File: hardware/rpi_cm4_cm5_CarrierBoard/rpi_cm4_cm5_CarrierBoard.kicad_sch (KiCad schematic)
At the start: 16 parts, among them J21 61300311121, J22 61300311121, J24 SM04B-SRSS-TB, U37 SN74LVC1G14DBVR

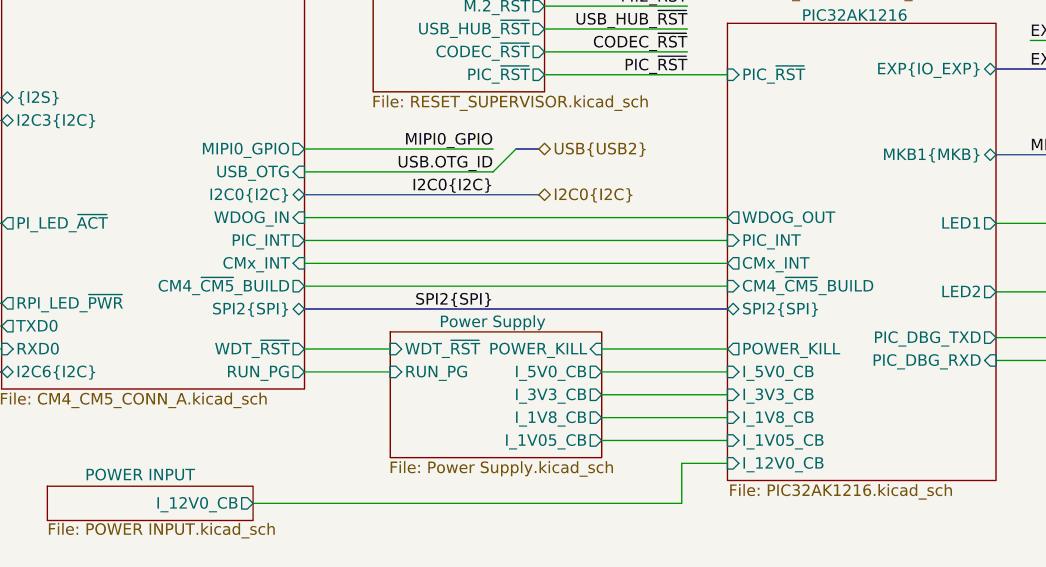
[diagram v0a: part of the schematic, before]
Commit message: Finished implementation of watchdog circuit All possible reset scenarios documented
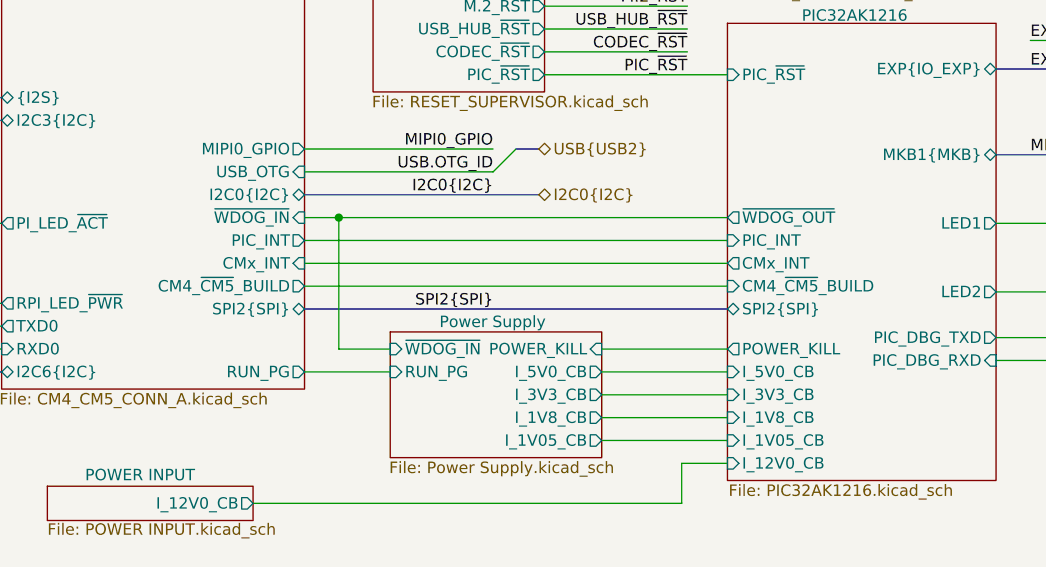
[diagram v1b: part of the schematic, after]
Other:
- sheet CM4_CM5_CONN_A ports: added ~{WDOG_IN}; removed WDOG_IN, WDT_~{RST}
- sheet PIC32AK1216 ports: added ~{WDOG_OUT}; removed WDOG_OUT
- sheet Power Supply ports: added ~{WDOG_IN}; removed WDT_~{RST}
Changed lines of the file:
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@@
 	)
 	(junction
+		(at 159.385 128.905)
+		(diameter 0)
+		(color 0 0 0 0)
+	)
+	(junction
 		(at 195.58 69.85)
 		(diameter 0)
@@
 	(wire
 		(pts
-			(xy 155.575 128.905) (xy 202.565 128.905)
+			(xy 155.575 128.905) (xy 159.385 128.905)
 		)
 		(stroke
@@
 	(wire
 		(pts
+			(xy 159.385 143.51) (xy 165.1 143.51)
+		)
+		(stroke
+			(width 0)
+			(type default)
+		)
+	)
+	(wire
+		(pts
 			(xy 182.245 105.41) (xy 198.12 105.41)
 		)
@@
 		)
 	)
+	(wire
+		(pts
+			(xy 159.385 128.905) (xy 159.385 143.51)
+		)
+		(stroke
+			(width 0)
+			(type default)
+		)
+	)
 	(bus
 		(pts
@@
 	(wire
 		(pts
+			(xy 159.385 128.905) (xy 202.565 128.905)
+		)
+		(stroke
+			(width 0)
+			(type default)
+		)
+	)
+	(wire
+		(pts
 			(xy 104.775 168.275) (xy 104.775 168.91)
 		)
@@
 	(wire
 		(pts
-			(xy 155.575 143.51) (xy 165.1 143.51)
-		)
-		(stroke
-			(width 0)
-			(type default)
-		)
-	)
-	(wire
-		(pts
 			(xy 45.72 91.44) (xy 121.92 91.44)
 		)
@@
 			)
 		)
-		(pin "WDOG_OUT" output
-			(at 202.565 128.905 180)
-			(effects
-				(font
-					(size 1.27 1.27)
-				)
-				(justify left)
-			)
-		)
 		(pin "CMx_INT" output
 			(at 202.565 133.985 180)
@@
 			)
 		)
+		(pin "~{WDOG_OUT}" output
+			(at 202.565 128.905 180)
+			(effects
+				(font
+					(size 1.27 1.27)
+				)
+				(justify left)
+			)
+		)
 		(instances
 			(project "rpi_cm4_cm5_CarrierBoard"
@@
 			)
 		)
-		(pin "WDT_~{RST}" input
+		(pin "~{WDOG_IN}" input
 			(at 165.1 143.51 180)
 			(effects
@@
 			)
 		)
-		(pin "WDOG_IN" input
-			(at 155.575 128.905 0)
-			(effects
-				(font
-					(size 1.27 1.27)
-				)
-				(justify right)
-			)
-		)
 		(pin "I2C3{I2C}" bidirectional
 			(at 121.92 118.11 180)
@@
 			)
 		)
-		(pin "WDT_~{RST}" output
-			(at 155.575 143.51 0)
+		(pin "~{WDOG_IN}" input
+			(at 155.575 128.905 0)
 			(effects
 				(font

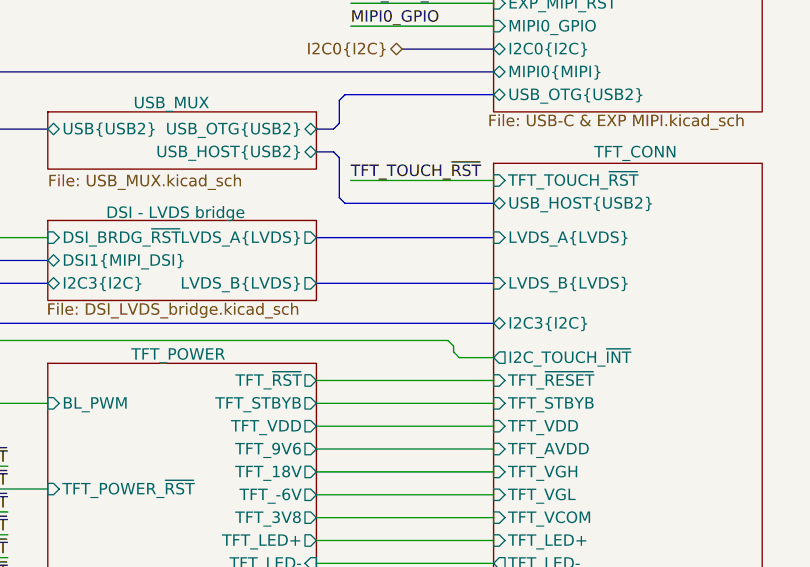
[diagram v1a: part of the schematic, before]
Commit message: Update schematics based on PCB preliminary placement Add preliminary design rules to PCB
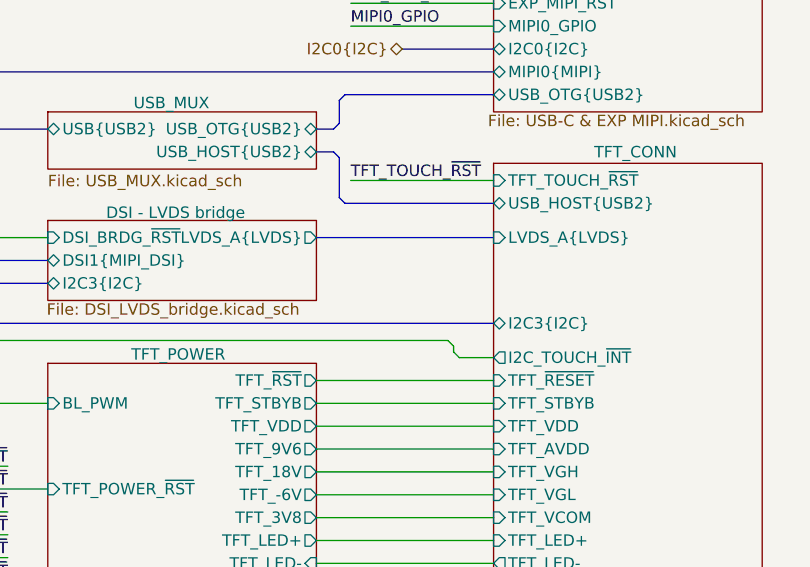
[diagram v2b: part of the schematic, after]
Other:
- sheet DSI - LVDS bridge ports: added none; removed LVDS_B{LVDS}
- sheet TFT_CONN ports: added none; removed LVDS_B{LVDS}
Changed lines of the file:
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@@
 	(bus
 		(pts
-			(xy 232.41 69.85) (xy 252.095 69.85)
-		)
-		(stroke
-			(width 0)
-			(type default)
-		)
-	)
-	(bus
-		(pts
 			(xy 155.575 67.31) (xy 202.565 67.31)
 		)
@@
 			)
 		)
-		(pin "LVDS_B{LVDS}" input
-			(at 252.095 69.85 180)
-			(effects
-				(font
-					(size 1.27 1.27)
-				)
-				(justify left)
-			)
-		)
 		(pin "I2C3{I2C}" bidirectional
 			(at 252.095 74.295 180)
@@
 			(effects
 				(font
-					(size 1.27 1.27)
-				)
-				(justify right)
-			)
-		)
-		(pin "LVDS_B{LVDS}" output
-			(at 232.41 69.85 0)
-			(effects
-				(font

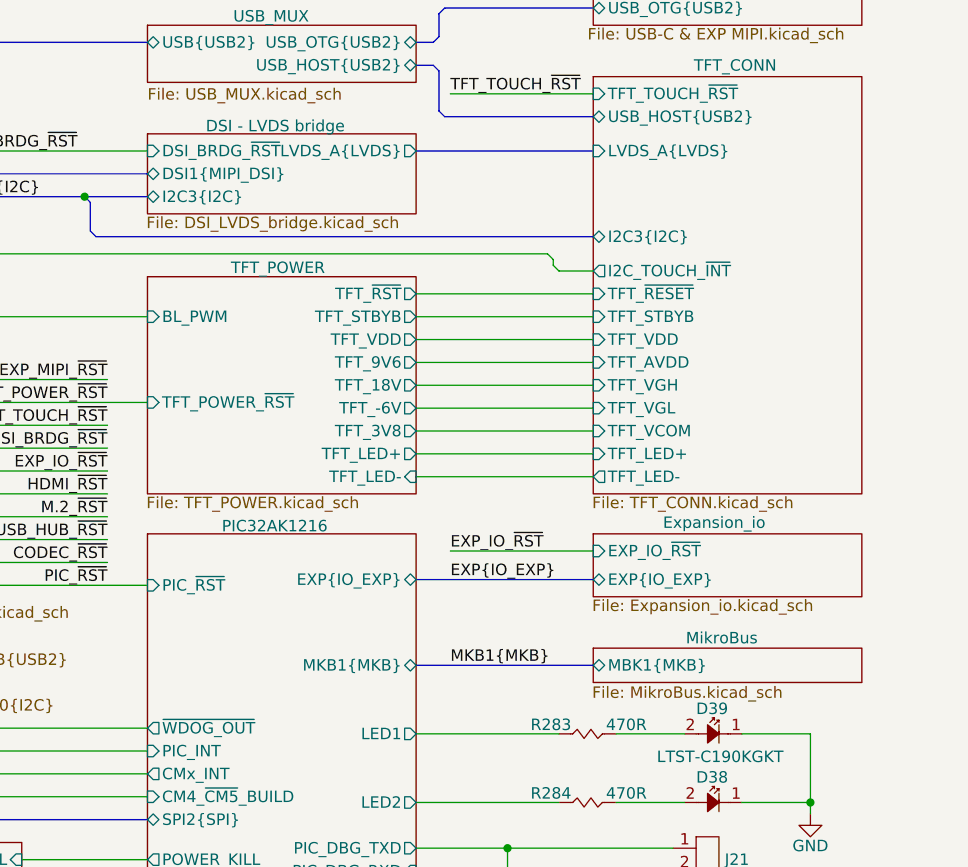
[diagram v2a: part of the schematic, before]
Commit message: Update PCB design rules for outer layers differential pairs Update preliminary component placement Update schematics based on PCB placement & remove duplicata / unnecessary components Update design notes and power table
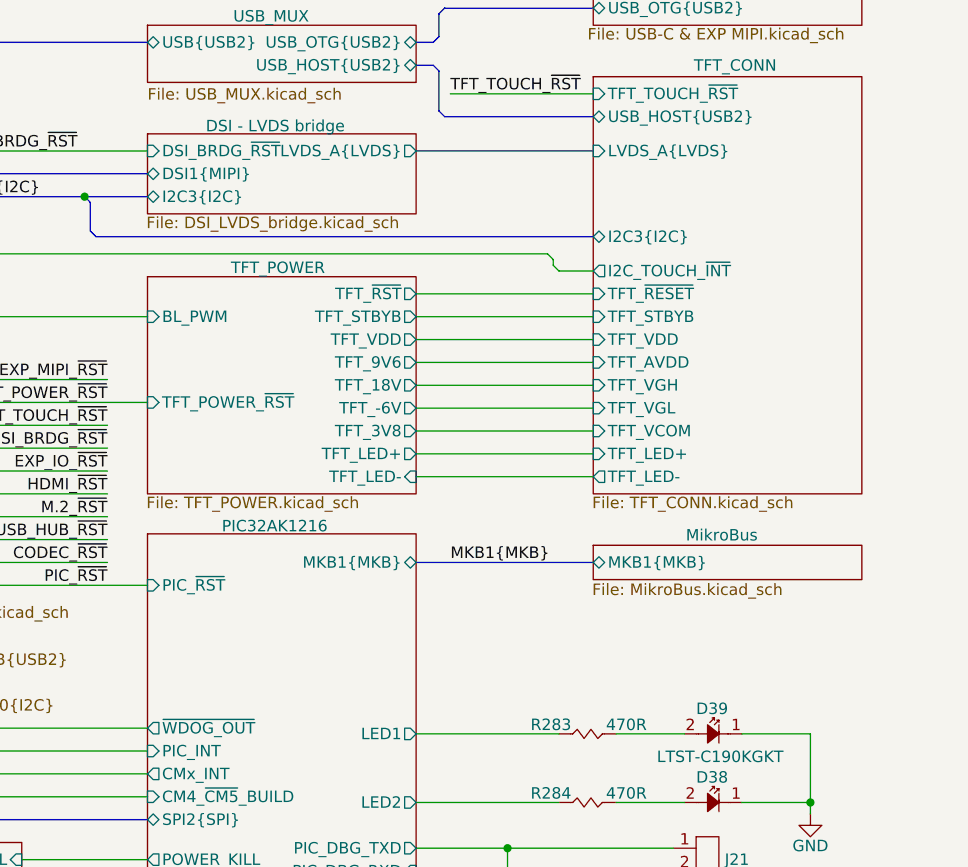
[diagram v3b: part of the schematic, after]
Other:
- removed sheet Expansion_io
- sheet DSI - LVDS bridge ports: added DSI1{MIPI}; removed DSI1{MIPI_DSI}
- sheet MikroBus ports: added MKB1{MKB}; removed MBK1{MKB}
- sheet PIC32AK1216 ports: added none; removed EXP{IO_EXP}
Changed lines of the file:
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@@
 	(bus
 		(pts
-			(xy 232.41 121.92) (xy 252.095 121.92)
+			(xy 232.41 110.49) (xy 252.095 110.49)
 		)
 		(stroke
@@
 	(wire
 		(pts
-			(xy 236.22 109.22) (xy 252.095 109.22)
-		)
-		(stroke
-			(width 0)
-			(type default)
-		)
-	)
-	(wire
-		(pts
 			(xy 247.65 76.835) (xy 247.015 76.2)
 		)
@@
 		)
 	)
-	(bus
-		(pts
-			(xy 232.41 112.395) (xy 252.095 112.395)
-		)
-		(stroke
-			(width 0)
-			(type default)
-		)
-	)
 	(wire
 		(pts
@@
 		)
 	)
-	(label "EXP_IO_~{RST}"
-		(at 236.22 109.22 0)
-		(effects
-			(font
-				(size 1.27 1.27)
-			)
-			(justify left bottom)
-		)
-	)
 	(label "I2C6.I2C_SDA"
 		(at 99.06 161.925 180)
@@
 		)
 	)
-	(label "EXP{IO_EXP}"
-		(at 236.22 112.395 0)
-		(effects
-			(font
-				(size 1.27 1.27)
-			)
-			(justify left bottom)
-		)
-	)
 	(label "SPI2{SPI}"
 		(at 176.53 139.065 180)
@@
 	)
 	(label "MKB1{MKB}"
-		(at 236.22 121.92 0)
+		(at 236.22 110.49 0)
 		(effects
 			(font
@@
 		)
 		(pin "MKB1{MKB}" bidirectional
-			(at 232.41 121.92 0)
+			(at 232.41 110.49 0)
 			(effects
 				(font
@@
 			)
 		)
-		(pin "EXP{IO_EXP}" bidirectional
-			(at 232.41 112.395 0)
-			(effects
-				(font
-					(size 1.27 1.27)
-				)
-				(justify right)
-			)
-		)
 		(pin "PIC_DBG_TXD" output
 			(at 232.41 142.24 0)
@@
 			)
 		)
-		(pin "DSI1{MIPI_DSI}" bidirectional
-			(at 202.565 67.31 180)
-			(effects
-				(font
-					(size 1.27 1.27)
-				)
-				(justify left)
-			)
-		)
 		(pin "I2C3{I2C}" bidirectional
 			(at 202.565 69.85 180)
@@
 			)
 		)
-		(instances
-			(project "rpi_cm4_cm5_CarrierBoard"
-				(path "/7dcdf741-90ca-4333-848c-806f4d64158e"
-					(page "6")
-				)
-			)
-		)
-	)
-	(sheet
-		(at 252.095 107.315)
-		(size 29.845 6.985)
-		(exclude_from_sim no)
-		(in_bom yes)
-		(on_board yes)
-		(dnp no)
-		(stroke
-			(width 0.1524)
-			(type solid)
-		)
-		(fill
-			(color 0 0 0 0.0000)
-		)
-		(property "Sheetname" "Expansion_io"
-			(at 259.842 106.807 0)
-			(effects
-				(font
-					(size 1.27 1.27)
-				)
-				(justify left bottom)
-			)
-		)
-		(property "Sheetfile" "Expansion_io.kicad_sch"
-			(at 251.968 114.554 0)
-			(effects
-				(font
-					(size 1.27 1.27)
-				)
-				(justify left top)
-			)
-		)
-		(pin "EXP{IO_EXP}" bidirectional
-			(at 252.095 112.395 180)
-			(effects
-				(font
-					(size 1.27 1.27)
-				)
-				(justify left)
-			)
-		)
-		(pin "EXP_IO_~{RST}" input
-			(at 252.095 109.22 180)
+		(pin "DSI1{MIPI}" bidirectional
+			(at 202.565 67.31 180)
 			(effects
 				(font
@@
 			(project "rpi_cm4_cm5_CarrierBoard"
 				(path "/7dcdf741-90ca-4333-848c-806f4d64158e"
-					(page "18")
+					(page "6")
 				)
 			)
@@
 	)
 	(sheet
-		(at 252.095 120.015)
+		(at 252.095 108.585)
 		(size 29.845 3.81)
 		(exclude_from_sim no)
@@
 		)
 		(property "Sheetname" "MikroBus"
-			(at 262.382 119.634 0)
+			(at 262.382 108.204 0)
 			(effects
 				(font
@@
 		)
 		(property "Sheetfile" "MikroBus.kicad_sch"
-			(at 251.968 124.206 0)
+			(at 251.968 112.776 0)
 			(effects
 				(font
@@
 			)
 		)
-		(pin "MBK1{MKB}" bidirectional
-			(at 252.095 121.92 180)
+		(pin "MKB1{MKB}" bidirectional
+			(at 252.095 110.49 180)
 			(effects
 				(font

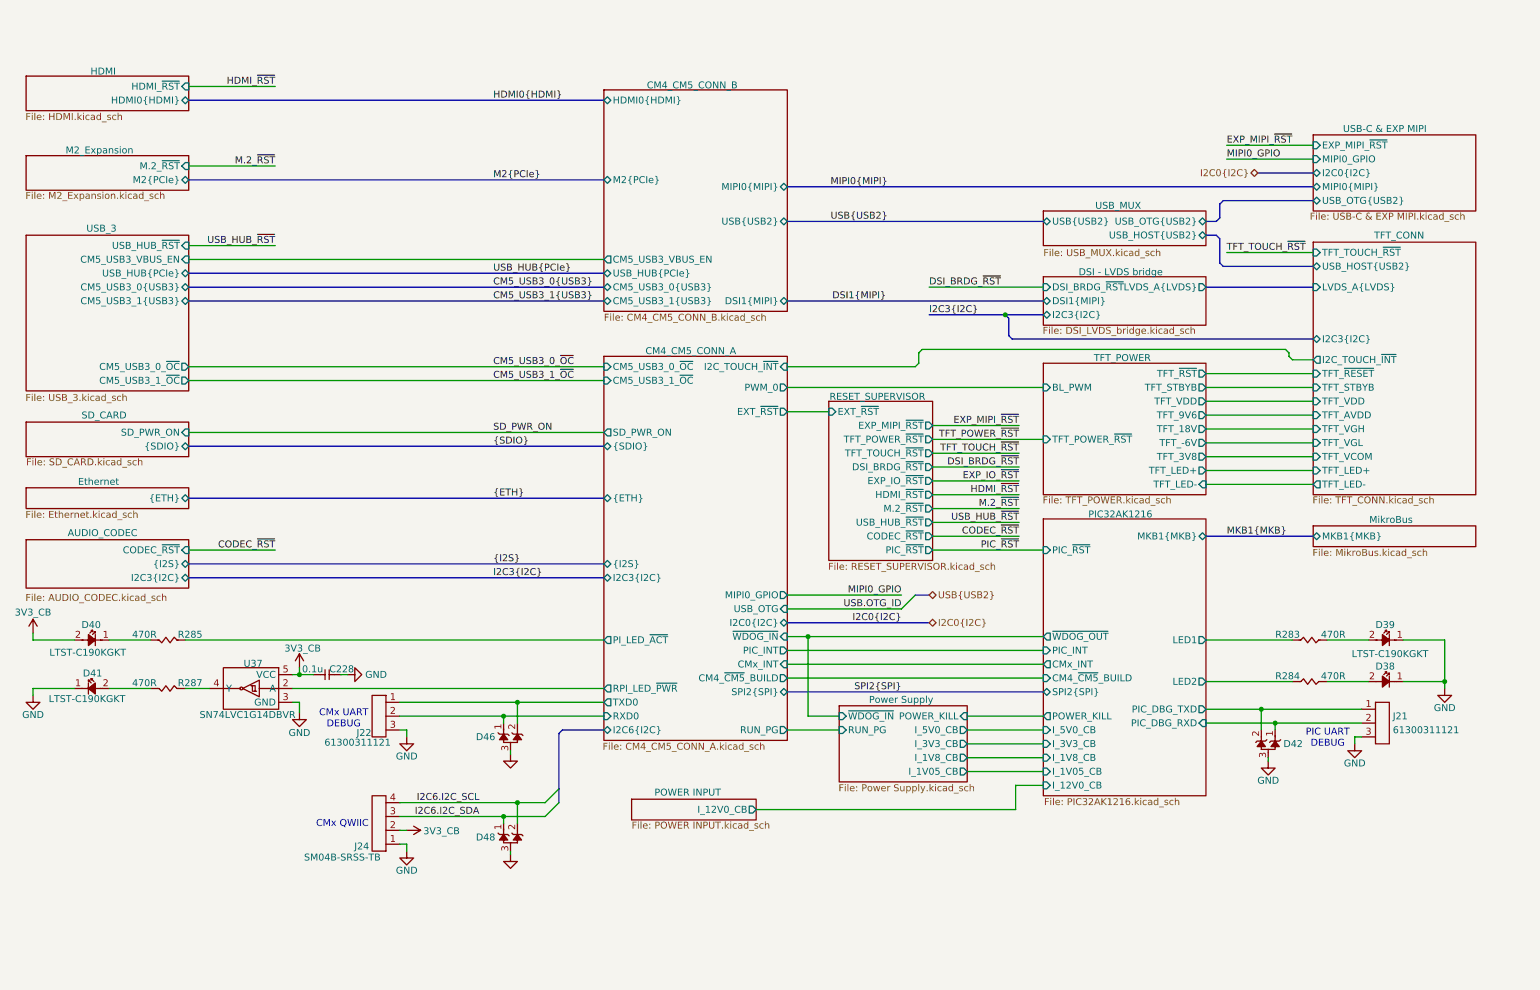
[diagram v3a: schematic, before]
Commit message: Document stackup Few changes to schematic based on preliminary PCB placement Update PinMux based on preliminary PCB placement and component positions
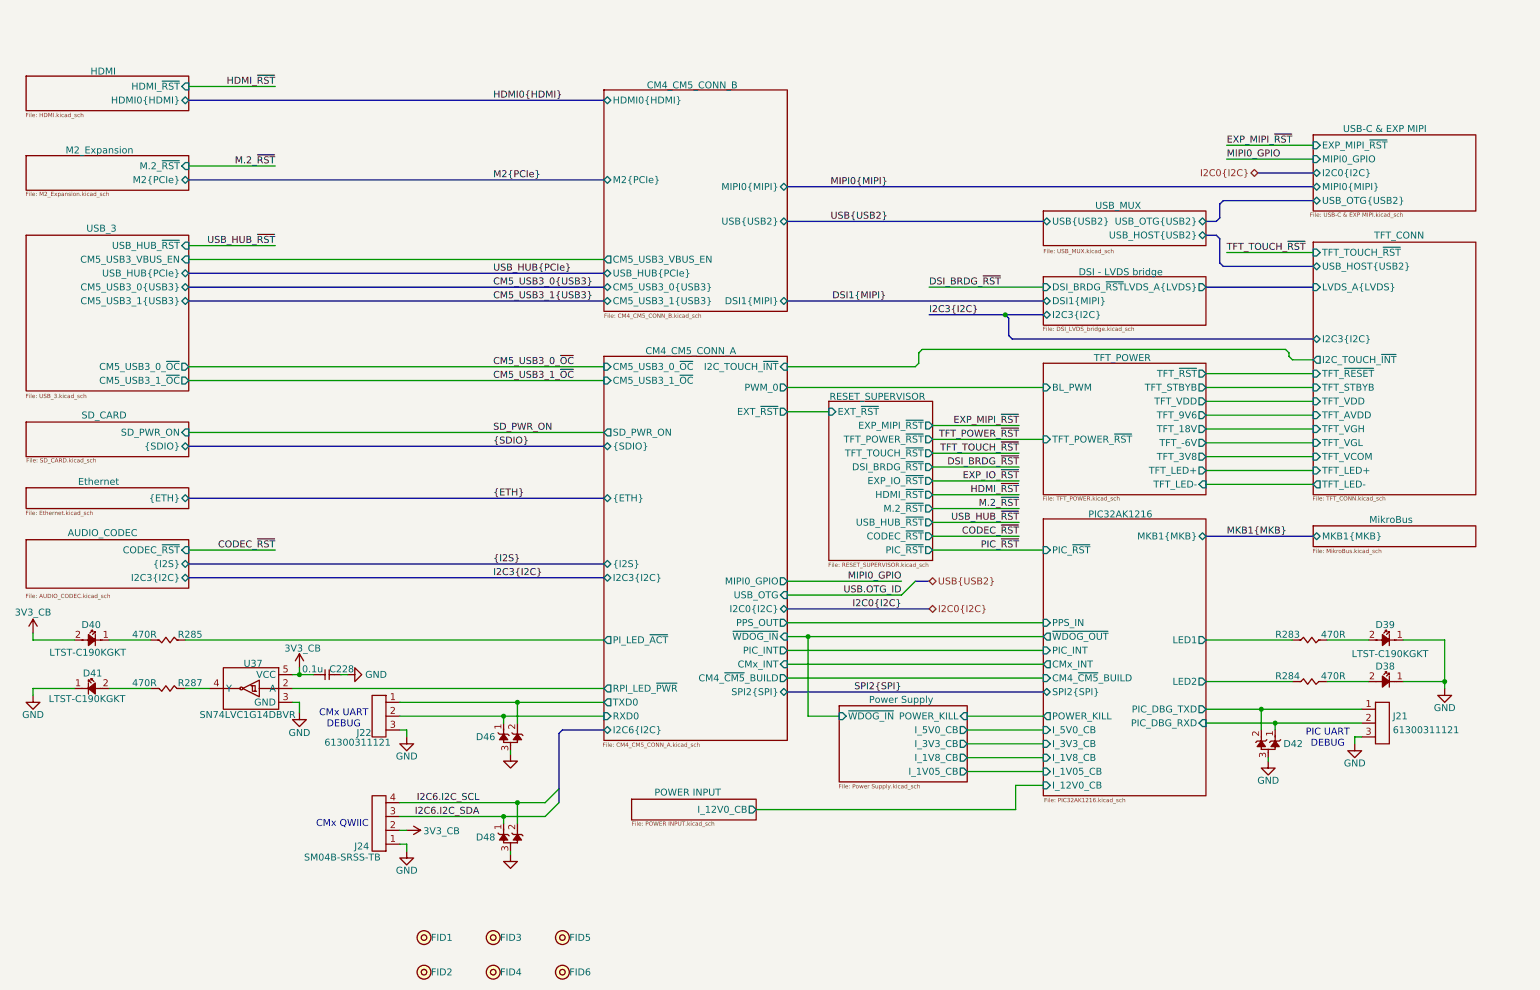
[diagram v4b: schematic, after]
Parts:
- added FID1, FID2, FID3, FID4, FID5, FID6: ~, FIDUCIAL, symbol KiCad_Lib_Symbols:FIDUCIAL
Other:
- sheet CM4_CM5_CONN_A ports: added PPS_OUT; removed RUN_PG
- sheet PIC32AK1216 ports: added PPS_IN; removed none
- sheet Power Supply ports: added none; removed RUN_PG
